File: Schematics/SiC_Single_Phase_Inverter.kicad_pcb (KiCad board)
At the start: 2 copper layers, 204.5 x 65.2 mm, 155 parts, among them IC1 F280049CPMSR, J1 23AH8786-Red, J10 464369202, J11 464379202, J12 43650-0418, J13 464369202, J14 464379202, J15 43650-0418, J16 464369202, J17 43650-0418, J18 43650-0418, J19 FTSH-105-01-LM-D-K, J2 23AH8785-Black, J20 43650-0418, J21 43650-0418, J22 43045-1212, J23 43045-1212, J3 23AH8786-Red, J4 23AH8785-Black, J5 464379202, J6 464369202, J7 464379202, J8 464369202, J9 464379202, Q1 STB10NK60ZT4, Q2 C3M0025065K, Q3 C3M0025065K, Q4 C3M0025065K, Q5 C3M0025065K, Q6 STB10NK60ZT4, U1 UCC21710QDWRQ1, U2 UCC21710QDWRQ1, U3 UCC21710QDWRQ1, U4 UCC21710QDWRQ1, U5 TR05S3V3, Y1 ABM8-20.000MHZ-B2-T

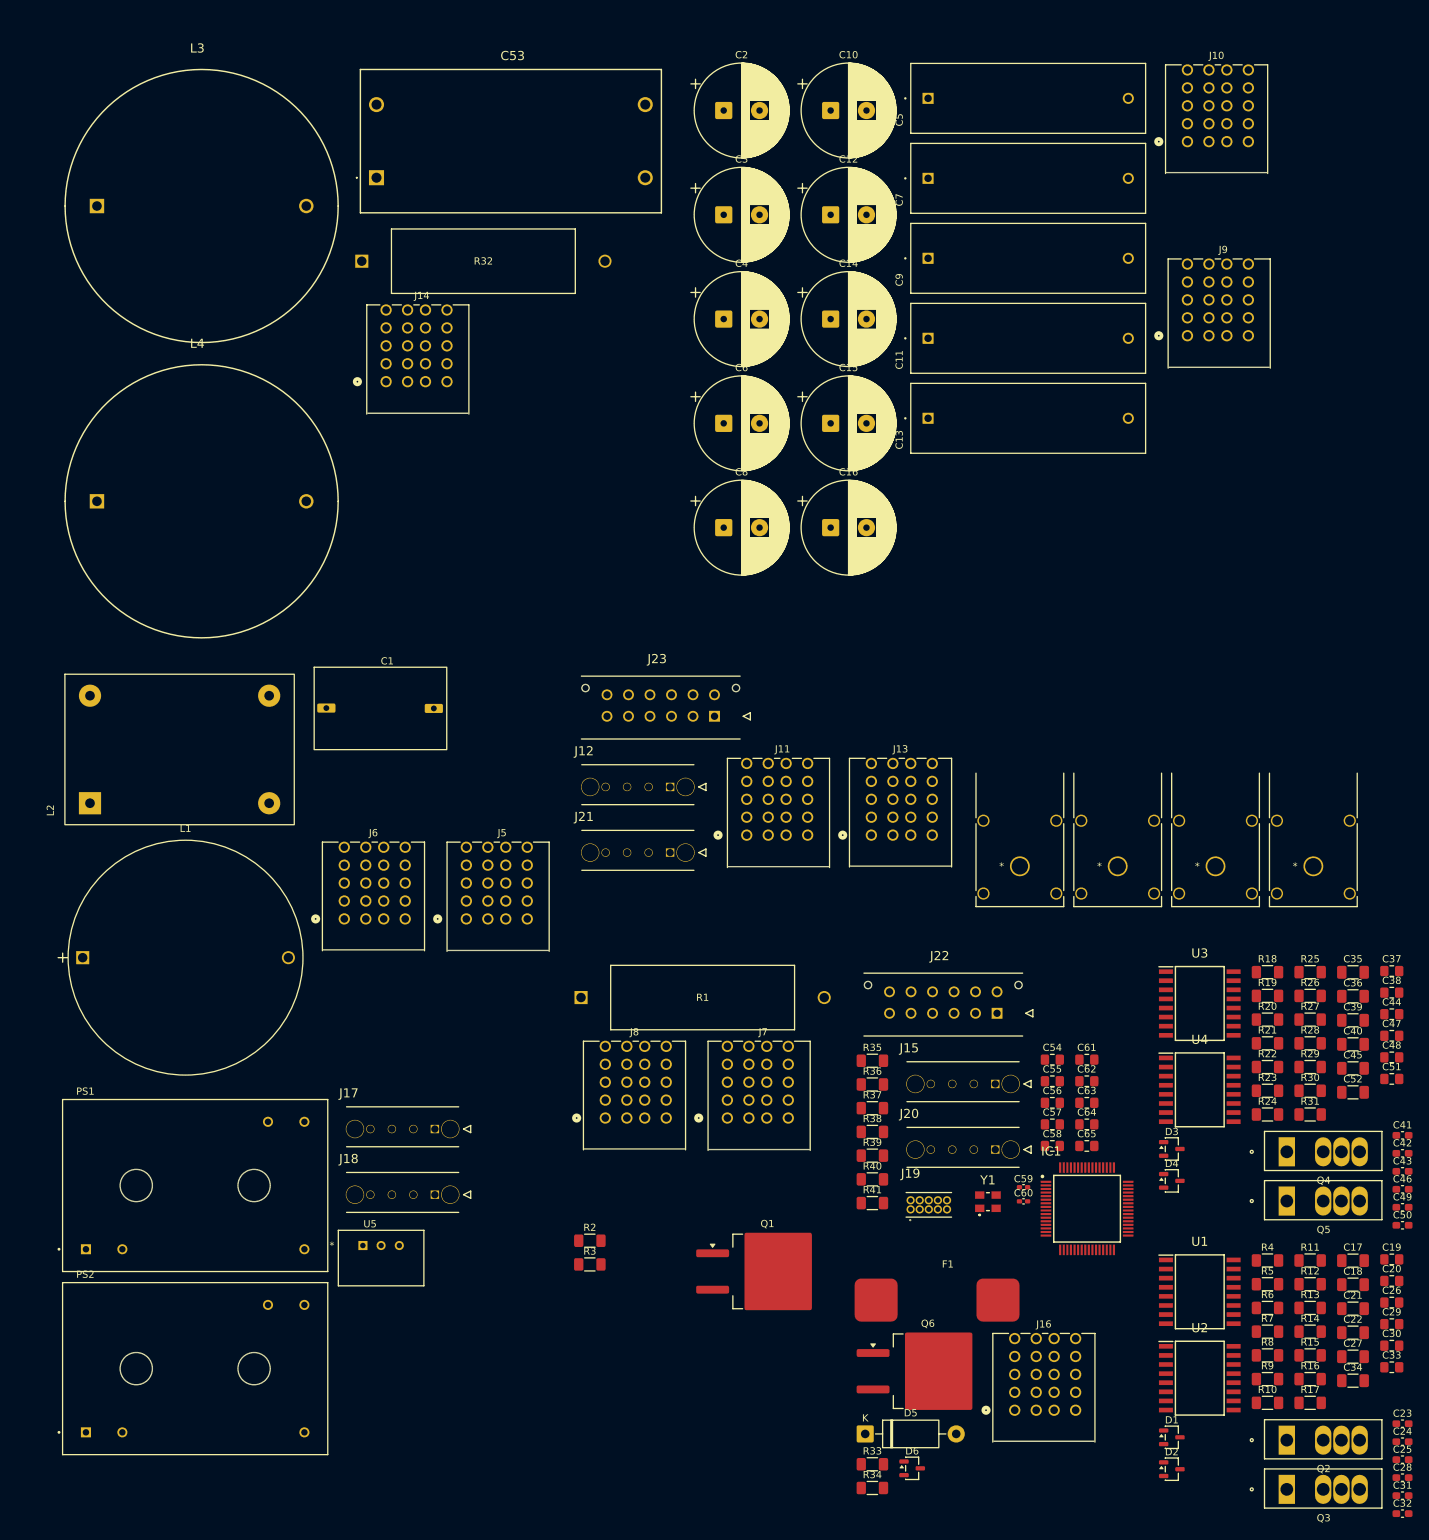
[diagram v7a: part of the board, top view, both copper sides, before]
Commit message: [WIP Controller Subsheet]
- Added USB sub sheet to allow use of a USB connection to controller
- Added USB parts for USB Circuit
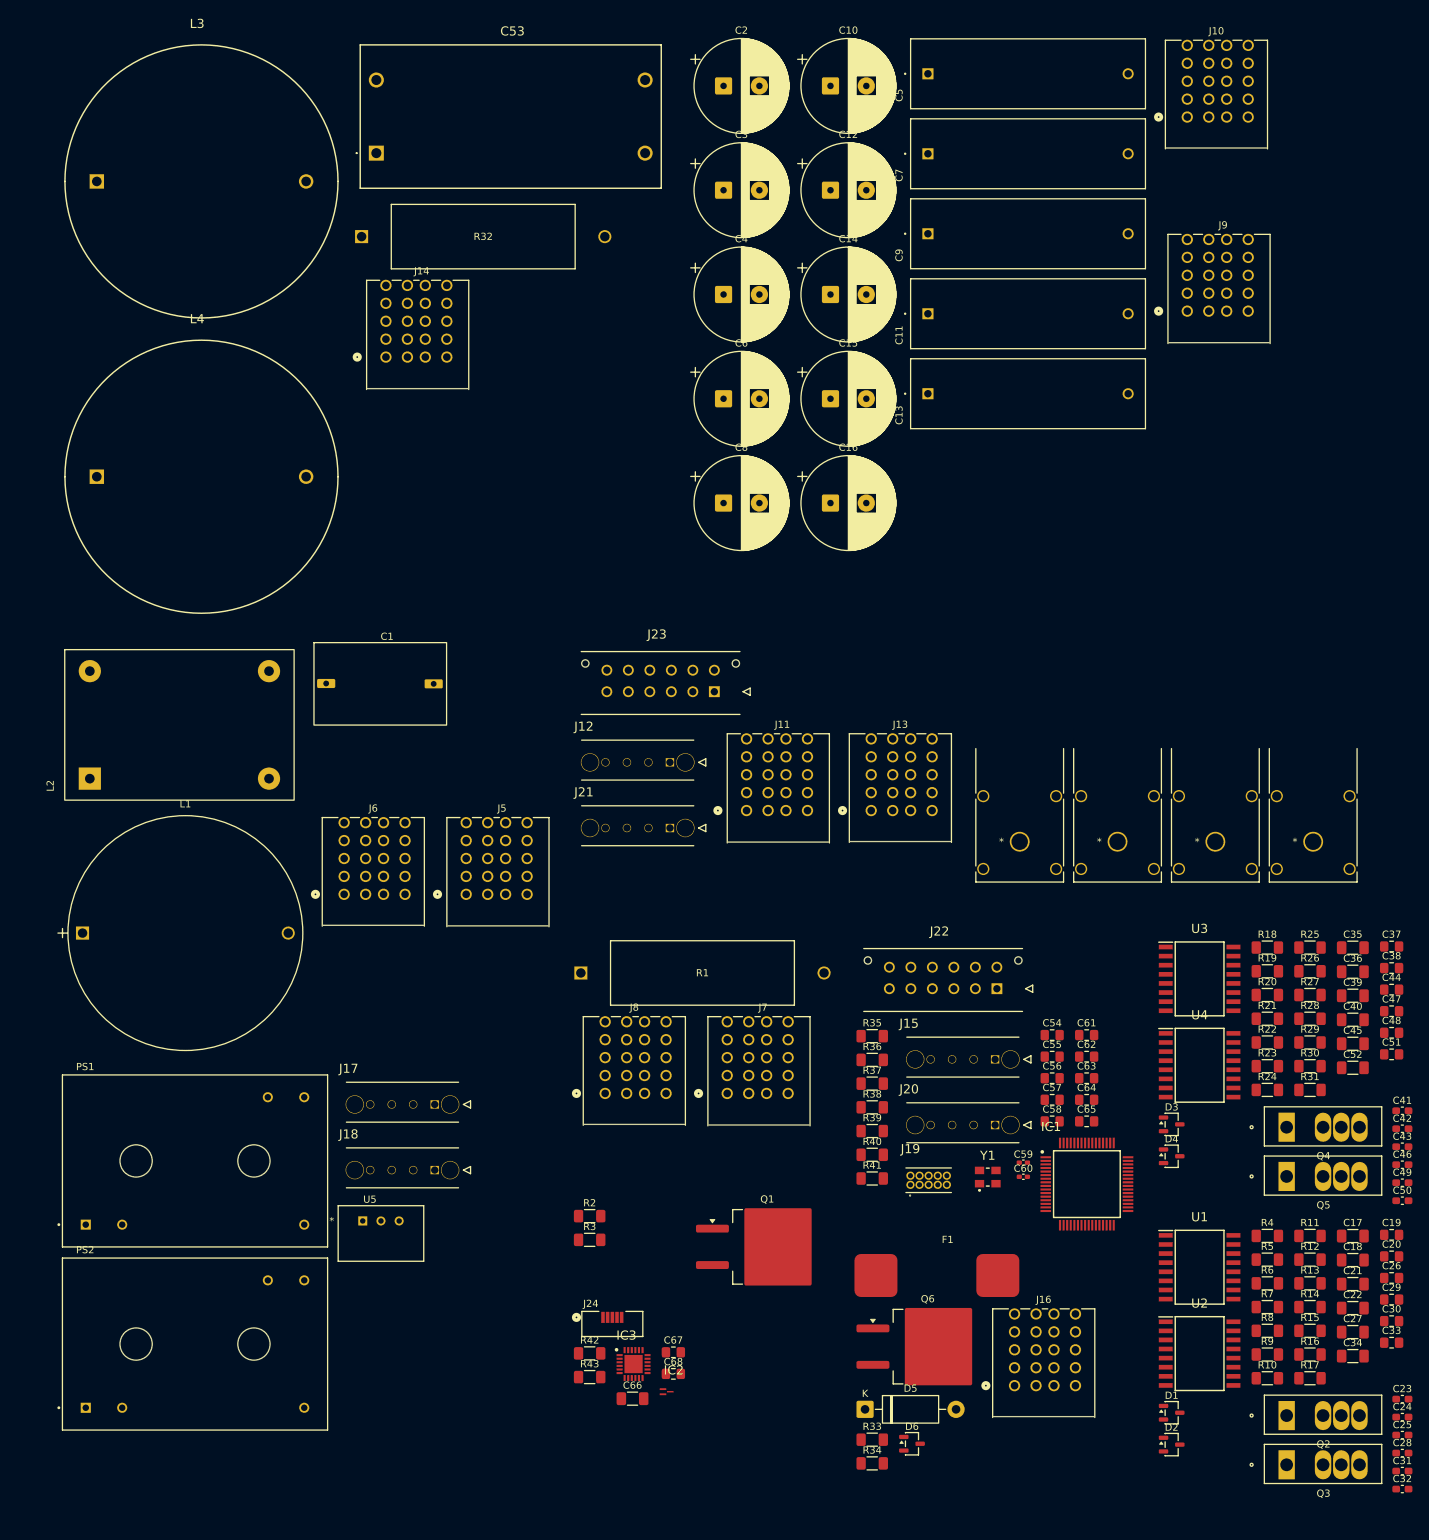
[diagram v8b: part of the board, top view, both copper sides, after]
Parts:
- added C66: 1 uF, Capacitor_SMD:C_1206_3216Metric_Pad1.33x1.80mm_HandSolder, F.Cu at (381.5, 197.7)
- added C67: 0.1 uF, Capacitor_SMD:C_0805_2012Metric_Pad1.18x1.45mm_HandSolder, F.Cu at (387.2, 191.2)
- added C68: 10 uF, Capacitor_SMD:C_0805_2012Metric_Pad1.18x1.45mm_HandSolder, F.Cu at (387.2, 194.2)
- added IC2: TPD2EUSB30ADRTR, SiC_Inverter:TPD2EUSB30ADRTR, F.Cu at (386.3, 196.7)
- added IC3: CP2102N-A02-GQFN24R, SiC_Inverter:CP2102N-A02-GQFN24R, F.Cu at (381.7, 192.8)
- added J24: 1051330011, SiC_Inverter:105133-0011, F.Cu at (378.7, 185.4)
- added R42: 0, Resistor_SMD:R_1206_3216Metric_Pad1.30x1.75mm_HandSolder, F.Cu at (375.6, 191.3)
- added R43: 100K, Resistor_SMD:R_1206_3216Metric_Pad1.30x1.75mm_HandSolder, F.Cu at (375.6, 194.7)
- moved C1 3.43 mm to (337.1, 103.7)
- moved C11 3.43 mm to (422.7, 46.3)
- moved C17 3.43 mm to (482.0, 175.0)
- moved C18 3.43 mm to (482.0, 178.3)
- moved C20 3.43 mm to (487.4, 177.8)
- moved C21 3.43 mm to (482.0, 181.7)
- moved C23 3.43 mm to (488.9, 197.7)
- moved C24 3.43 mm to (488.9, 200.2)
- moved C26 3.43 mm to (487.4, 180.8)
- moved C27 3.43 mm to (482.0, 188.4)
- moved C28 3.43 mm to (488.9, 205.2)
- moved C30 3.43 mm to (487.4, 186.8)
- moved C31 3.43 mm to (488.9, 207.8)
- moved C33 3.43 mm to (487.4, 189.8)
- moved C34 3.43 mm to (482.0, 191.7)
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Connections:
- net /Controller/SCIRXDA renamed /Con_SCIRXDA
- IC1 pad 2: /Controller/SCITXDA -> /Con_SCITXDA
